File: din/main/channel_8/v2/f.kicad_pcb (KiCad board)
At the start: 2 copper layers, 76.8 x 81.3 mm, 16 parts, among them J1 fm16_i, J10 wrs_i, J11 selector4_i, J12 Bus88_2x14, J2 dio_channel_i, J3 dio_channel_i, J4 dio_channel_i, J5 dio_channel_i, J6 dio_channel_i, J7 dio_channel_i, J8 dio_channel_i, J9 dio_channel_i, U1 74LS245

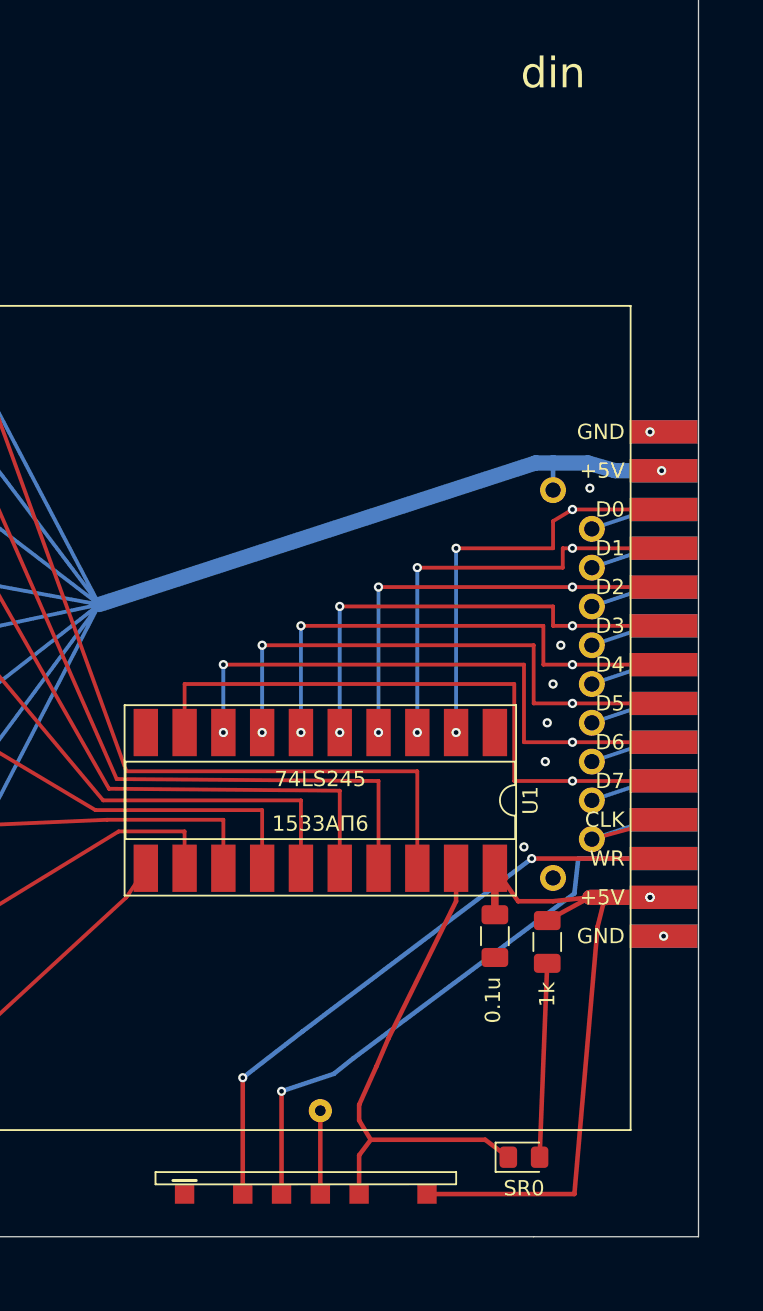
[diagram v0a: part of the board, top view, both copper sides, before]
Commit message: voltage regulator for each module
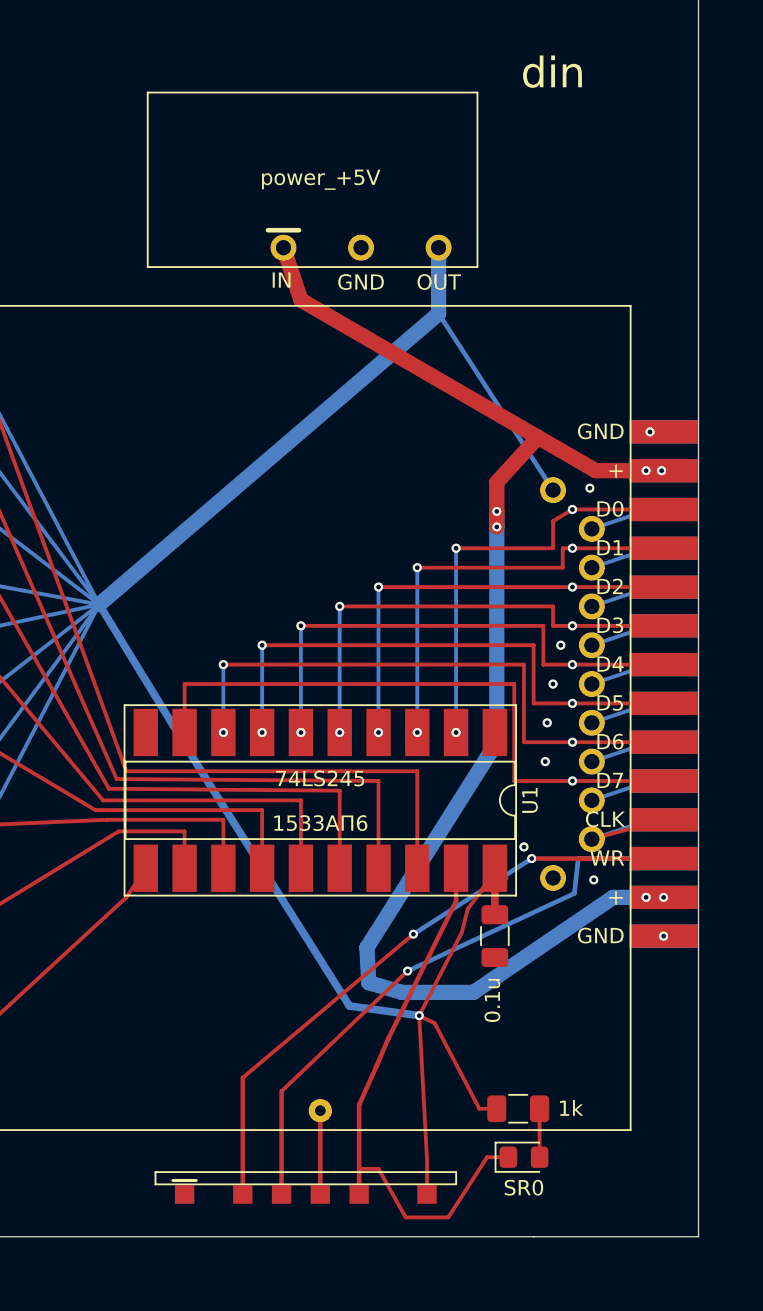
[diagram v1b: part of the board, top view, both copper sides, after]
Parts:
- added J13: bus_i, plc88:bus_im, F.Cu at (108.8, 59.1)
- J12: value Bus88_2x14 -> power_+5V; footprint 1my_elements:Bus88_2x14 -> plc88:power_i
- moved J12 38.3 mm to (77.6, 36.8)
- moved R1 11.1 mm to (99.3, 103.4), turned to 0 degrees
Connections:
- J12 pad 1: GND -> VPBUS
- J12 pad 2: GND -> +5V
- J12 pad 3: +5V -> GND
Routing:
- net VPBUS: track 0.00 -> 91.9 mm, vias 0 -> 6
- net +5V: track 310.8 -> 333.5 mm, vias 11 -> 9
- net Net-(D1-Pad2): track 12.7 -> 3.18 mm
- net SR0: track 32.6 -> 36.6 mm
- net GND: vias 9 -> 10
